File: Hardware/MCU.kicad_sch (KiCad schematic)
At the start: 26 parts, among them Q1 Q_NMOS_GSD, SW1 SW_SPST, SW3 SW_Push, SW4 SW_Push

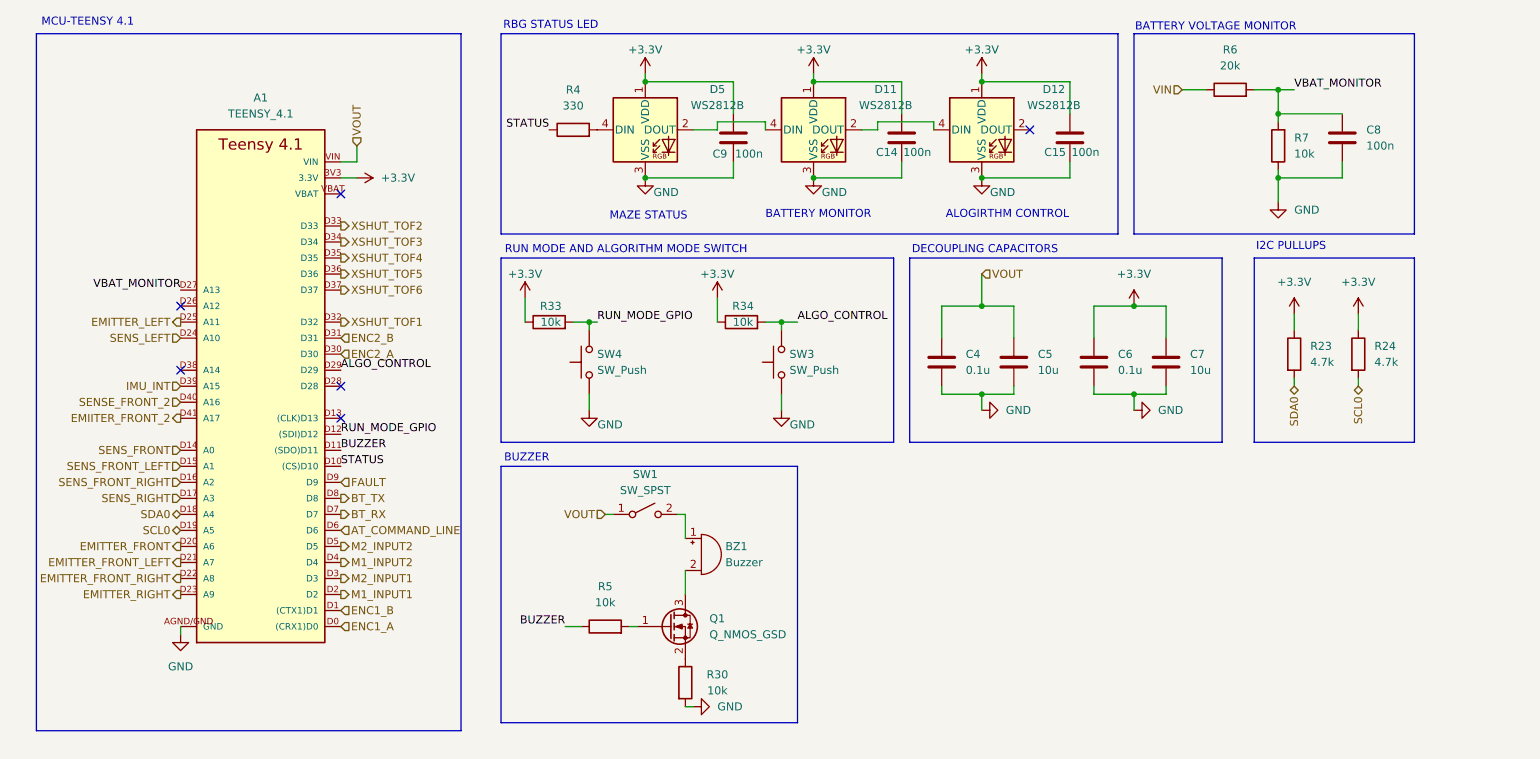
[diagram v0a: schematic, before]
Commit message: Schematic updated with buck and motor driver breakout boards
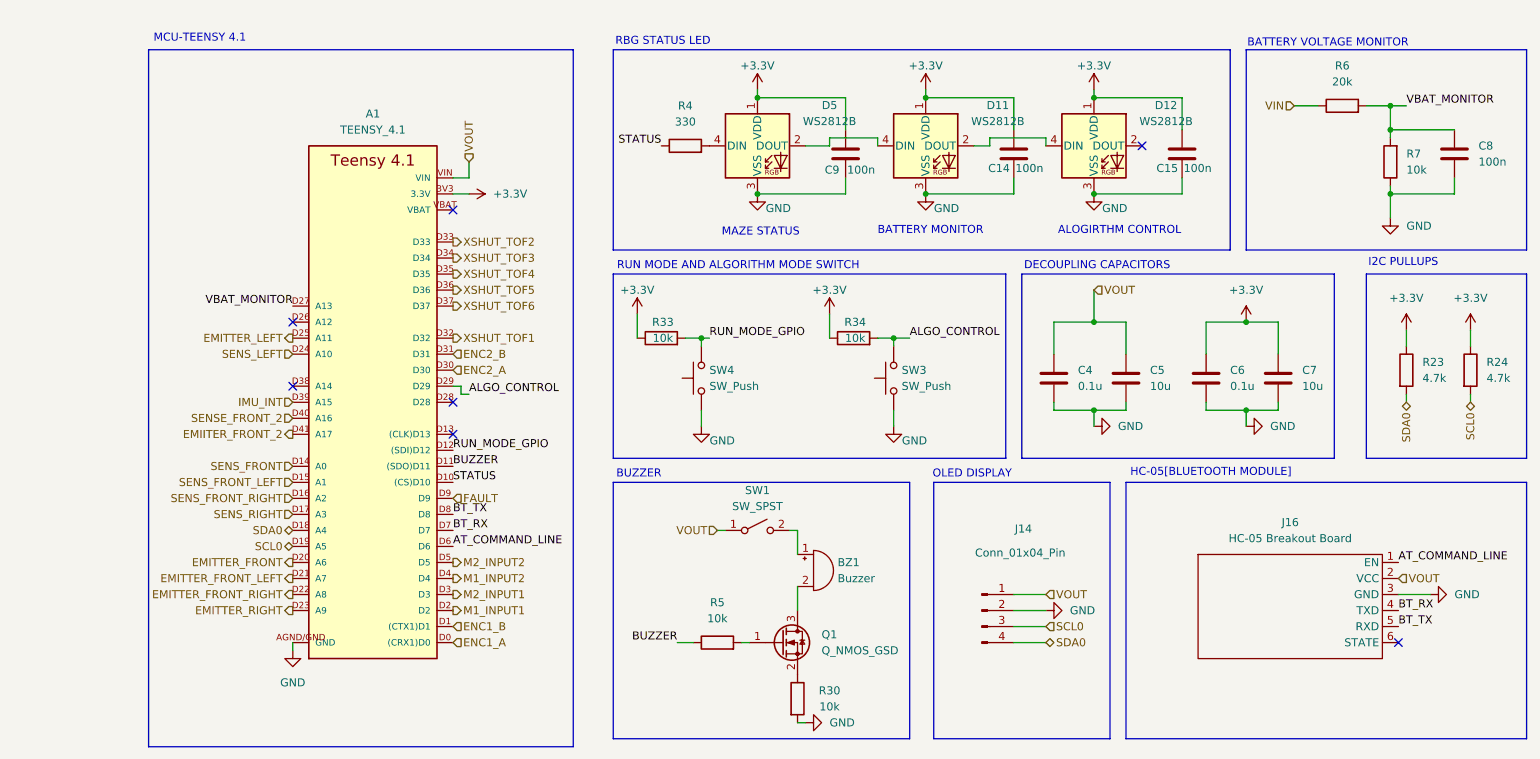
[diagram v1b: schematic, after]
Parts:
- added J14: Conn_01x04_Pin, symbol Connector:Conn_01x04_Pin
- added J16: HC-05 Breakout Board, symbol HSM_Symbols:HC-05_Breakout
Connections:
- net AT_COMMAND_LINE: now also J16.1 (EN)
- net BT_RX: now also J16.4 (TXD)
- net BT_TX: now also J16.5 (RXD)
- net GND: now also J14.2 (Pin_2), J16.3 (GND)
- net SCL0: now also J14.3 (Pin_3)
- net SDA0: now also J14.4 (Pin_4)
- net VOUT: now also J14.1 (Pin_1), J16.2 (VCC)
- no-connect marks 6 -> 7
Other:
- note added: "HC-05[BLUETOOTH MODULE]"
- note added: "OLED DISPLAY"
- moved on the sheet: A1, BZ1, C14, C15, C4, C5, C6, C7, C8, C9, D11, D12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

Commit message: Switches changed,added low pass filters, emitter caps
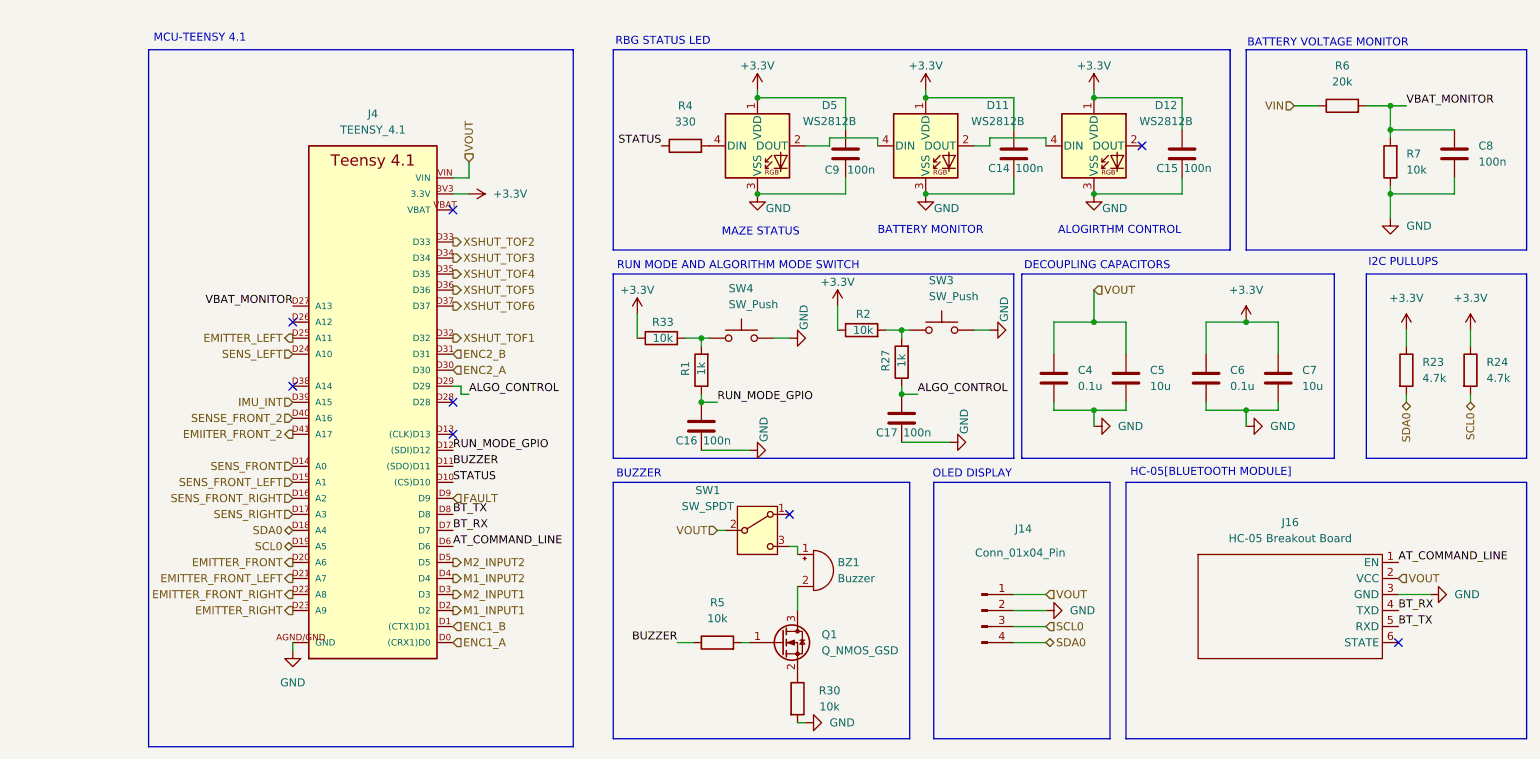
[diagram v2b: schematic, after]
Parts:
- removed R34: 10k, symbol Device:R
- removed SW1: SW_SPST, symbol Switch:SW_SPST
- added C16, C17: 100n, Capacitor_SMD:C_0603_1608Metric, symbol Device:C
- added R1, R27: 1k, Resistor_SMD:R_0603_1608Metric, symbol Device:R
- added R2: 10k, Resistor_SMD:R_0603_1608Metric, symbol Device:R
- added SW1: SW_SPDT, symbol Switch:SW_SPDT
- BZ1: footprint (none) -> Buzzer_Beeper:Buzzer_12x9.5RM7.6
- C14, C15, C4, C5, C6, C7, C8, C9: footprint (none) -> Capacitor_SMD:C_0603_1608Metric
- J14: footprint (none) -> Connector_PinSocket_2.54mm:PinSocket_1x04_P2.54mm_Vertical
- J16: footprint (none) -> Connector_PinSocket_2.54mm:PinSocket_1x06_P2.54mm_Vertical
- Q1: footprint (none) -> Package_TO_SOT_SMD:SOT-23
- R23, R24, R30, R33, R4, R5, R6, R7: footprint (none) -> Resistor_SMD:R_0603_1608Metric
- SW3, SW4: footprint (none) -> Button_Switch_SMD:SW_SPST_TL3342
- renumbered A1 to J4
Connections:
- net +3.3V: now also R2.1
- net ALGO_CONTROL: now also C17.1, R27.1; no longer SW3.2
- net GND: now also SW3.2, SW4.2, C16.2, C17.2; no longer SW3.1, SW4.1
- net RUN_MODE_GPIO: now also C16.1, R1.1; no longer R33.2, SW4.2
- net VOUT: now also SW1.2 (B)
- net at BZ1.1 (+): now also SW1.3 (C)
- new net: R1.2, R33.2, SW4.1
- new net: R2.2, R27.2, SW3.1
- no-connect marks 7 -> 8
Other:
- moved on the sheet: SW4

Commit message: Added KiCad PCB files
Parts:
- SW1: footprint (none) -> Button_Switch_SMD:SW_SPDT_CK_JS102011SAQN
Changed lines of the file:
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@@
 			)
 		)
-		(property "Footprint" ""
+		(property "Footprint" "Button_Switch_SMD:SW_SPDT_CK_JS102011SAQN"
 			(at 137.16 115.57 0)
 			(effects

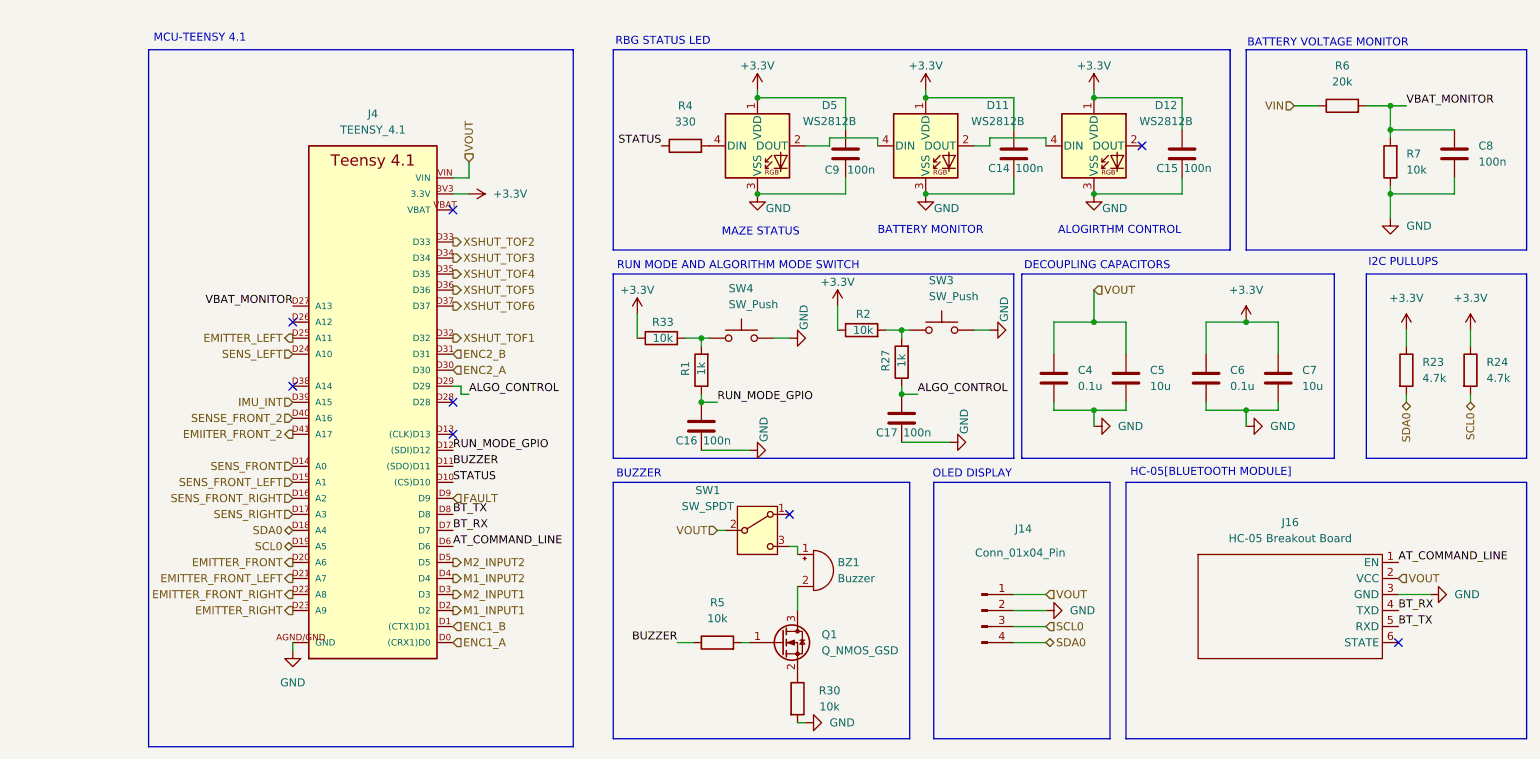
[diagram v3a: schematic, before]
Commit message: Added the mounting holes, kill iwtch for the moto,removed resistors from xshut, and some others
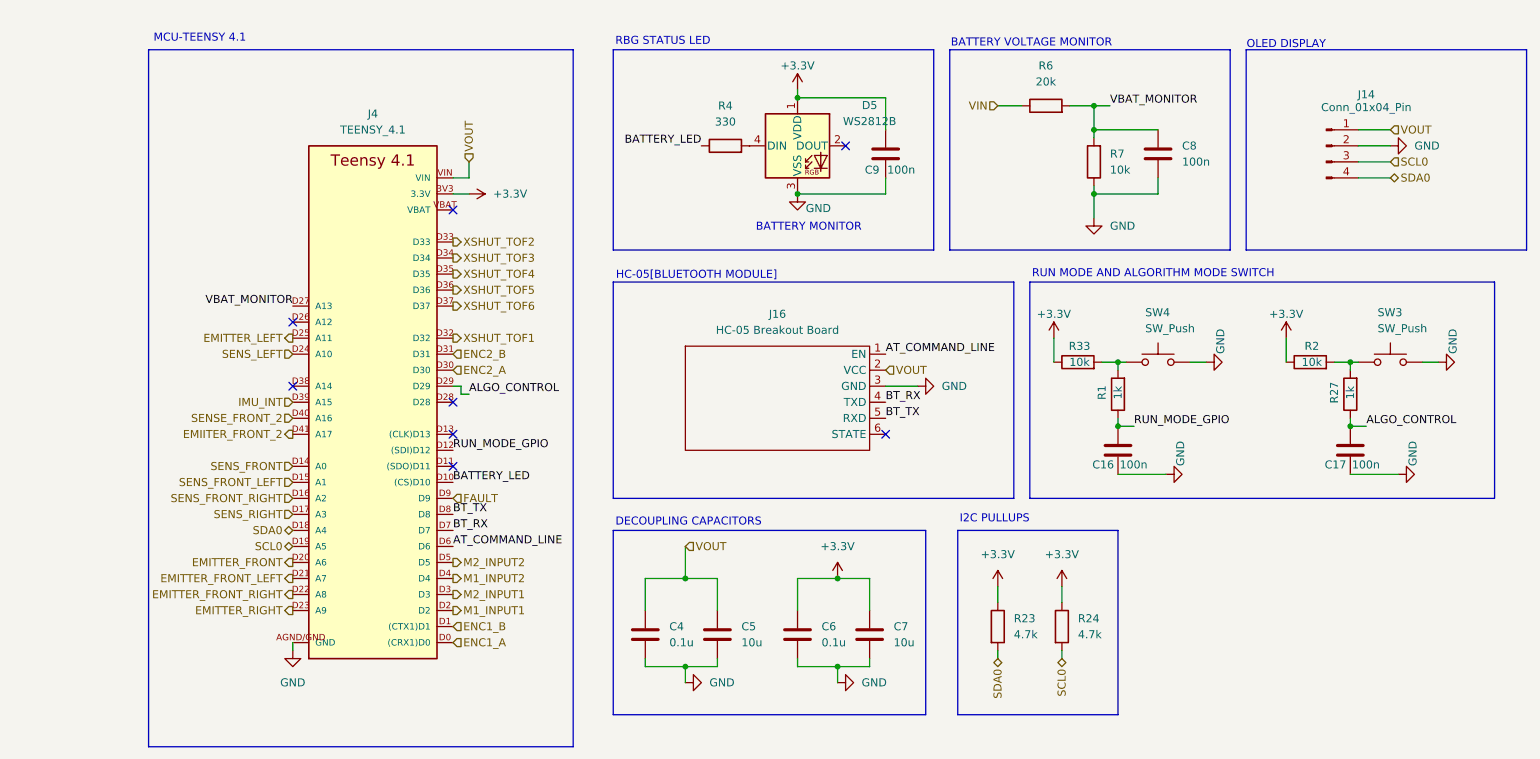
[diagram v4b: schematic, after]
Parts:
- removed BZ1: Buzzer, Buzzer_Beeper:Buzzer_12x9.5RM7.6, symbol Device:Buzzer
- removed C14, C15: 100n, Capacitor_SMD:C_0603_1608Metric, symbol Device:C
- removed D11, D12: WS2812B, LED_SMD:LED_WS2812B_PLCC4_5.0x5.0mm_P3.2mm, symbol LED:WS2812B
- removed Q1: Q_NMOS_GSD, Package_TO_SOT_SMD:SOT-23, symbol Transistor_FET:Q_NMOS_GSD
- removed R30, R5: 10k, Resistor_SMD:R_0603_1608Metric, symbol Device:R
- removed SW1: SW_SPDT, Button_Switch_SMD:SW_SPDT_CK_JS102011SAQN, symbol Switch:SW_SPDT
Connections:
- net BUZZER: no longer names the net of J4.D11 ((SDO)D11)
- net STATUS renamed BATTERY_LED
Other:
- note removed: "ALOGIRTHM CONTROL"
- note removed: "BUZZER"
- note removed: "MAZE STATUS"
- moved on the sheet: C16, C17, C4, C5, C6, C7, C8, C9, D5, J14, J16, R1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

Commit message: 1)PCB tracing continued, power traces need to verified,signal traces almost done except xshut, need to verify drv8833 dimesnions, should resolve teensy 4.1 error, switches footprint need to be changed. 2) changed schematic for optimum tracing in pcb editor,removed oled and added one more extra i2c bus to prevent i2c locking
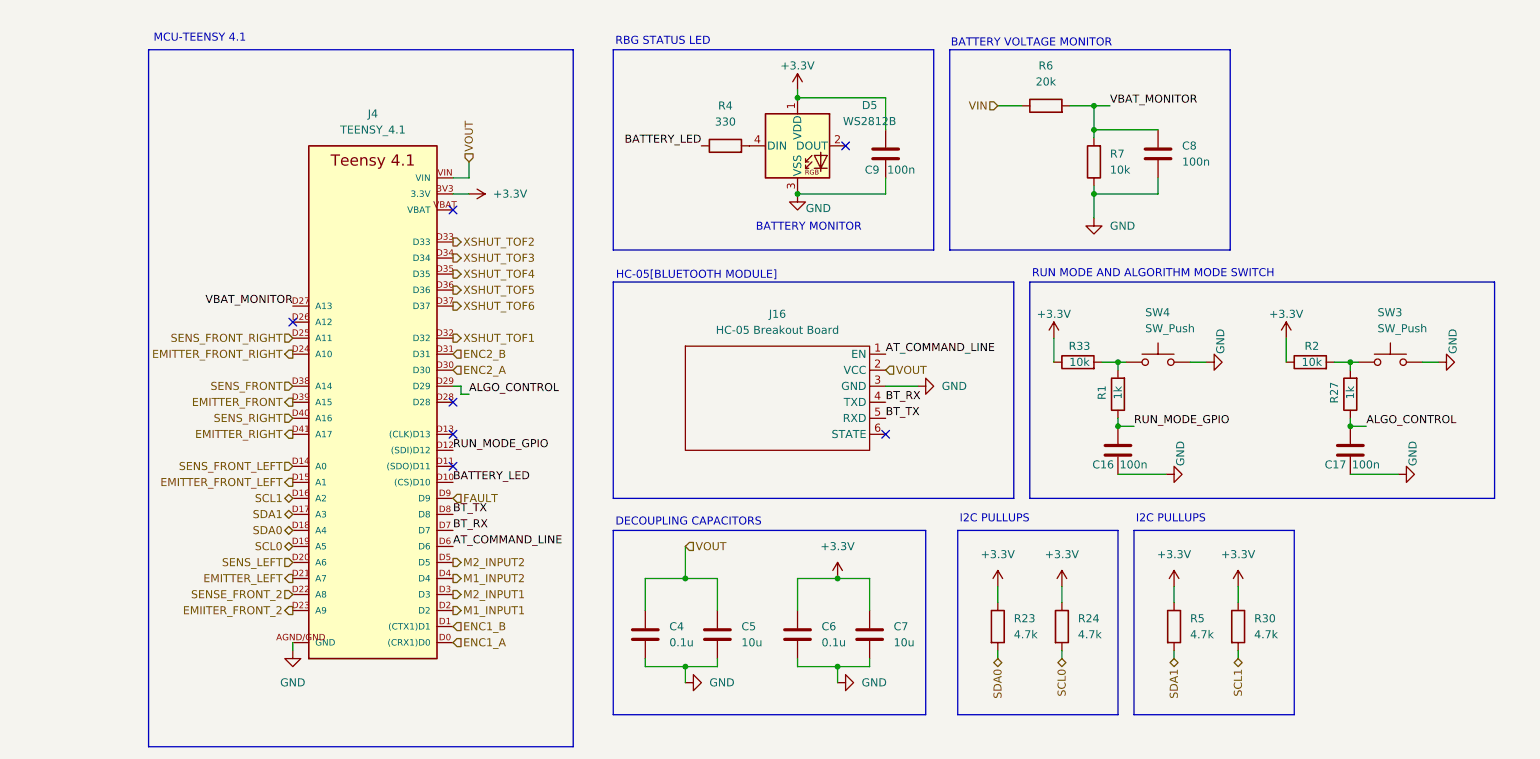
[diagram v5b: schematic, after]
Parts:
- removed J14: Conn_01x04_Pin, Connector_PinSocket_2.54mm:PinSocket_1x04_P2.54mm_Vertical, symbol Connector:Conn_01x04_Pin
- added R30, R5: 4.7k, Resistor_SMD:R_0603_1608Metric, symbol Device:R
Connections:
- net IMU_INT is gone; now on net EMITTER_FRONT: J4.D39 (A15)
- net +3.3V: now also R30.1, R5.1
- net EMIITER_FRONT_2: now also J4.D23 (A9); no longer J4.D41 (A17)
- net EMITTER_FRONT: no longer J4.D20 (A6)
- net EMITTER_FRONT_LEFT: now also J4.D15 (A1); no longer J4.D21 (A7)
- net EMITTER_FRONT_RIGHT: now also J4.D24 (A10); no longer J4.D22 (A8)
- net EMITTER_LEFT: now also J4.D21 (A7); no longer J4.D25 (A11)
- net EMITTER_RIGHT: now also J4.D41 (A17); no longer J4.D23 (A9)
- net SENSE_FRONT_2: now also J4.D22 (A8); no longer J4.D40 (A16)
- net SENS_FRONT: now also J4.D38 (A14); no longer J4.D14 (A0)
- net SENS_FRONT_LEFT: now also J4.D14 (A0); no longer J4.D15 (A1)
- net SENS_FRONT_RIGHT: now also J4.D25 (A11); no longer J4.D16 (A2)
- net SENS_LEFT: now also J4.D20 (A6); no longer J4.D24 (A10)
- net SENS_RIGHT: now also J4.D40 (A16); no longer J4.D17 (A3)
- new net SCL1: J4.D16 (A2), R30.2
- new net SDA1: J4.D17 (A3), R5.2
- no-connect marks 8 -> 7
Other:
- note removed: "OLED DISPLAY"

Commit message: Final updated pcb and schematic before dfm check
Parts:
- C16, C17, C4, C5, C6, C7, C8, C9: footprint Capacitor_SMD:C_0603_1608Metric -> Capacitor_SMD:C_0603_1608Metric_Pad1.08x0.95mm_HandSolder
- R1, R2, R23, R24, R27, R30, R33, R4, R5, R6, R7: footprint Resistor_SMD:R_0603_1608Metric -> Resistor_SMD:R_0603_1608Metric_Pad0.98x0.95mm_HandSolder
- SW3, SW4: footprint Button_Switch_SMD:SW_SPST_TL3342 -> Button_Switch_THT:SW_PUSH_6mm_H5mm
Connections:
- net RST_GPIO: now reaches J4.D11 ((SDO)D11)
- net INT_GPIO: now reaches J4.D26 (A12)
- net VIN renamed VBAT
- net VOUT renamed +5V
- no-connect marks 7 -> 5
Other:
- moved on the sheet: C16, C17, C4, C5, C6, C7, C8, C9, D5, J16, R1, R2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
